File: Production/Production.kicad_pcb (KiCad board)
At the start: 2 copper layers, 8.6 x 4.5 mm, 38 parts, among them IC1 MAX3323EEPE+, J1 530480510, J13 FH34SRJ-16S-0.5SH_50_, J2 530480410, J3 USB4085-GF-A_REVB, J6 Program, U1 BD33FC0FP-E2, U2 ADR02AUJZ-REEL7, U3 ATSAMD21G18A-AUT, Y1 32.768, 12.5pF

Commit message: Solid layout, could be better
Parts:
- removed S1: RESET, PVA1EEH21.2NV2:PVA1EEH212NV2
- removed S2: SET, PVA1EEH21.2NV2:PVA1EEH212NV2
- removed S3: SOFT, PVA1EEH21.2NV2:PVA1EEH212NV2
- added RESET1: B3U-1000P, Button_Switch_SMD:SW_SPST_B3U-1000P, F.Cu at (99.5, 93.5)
- added SET1: TS01-66-73-BK-160-D, TS01-66-73-BK-160-D:TS016673BK160D, F.Cu at (116.8, 68.8)
- added SOFT1: TS01-66-73-BK-160-D, TS01-66-73-BK-160-D:TS016673BK160D, F.Cu at (90.2, 68.8)
- J2: footprint Connector_Molex:Molex_PicoBlade_53048-0410_1x04_P1.25mm_Horizontal -> Connector_Molex_2:Molex_PicoBlade_53048-0410_1x04_P1.25mm_Horizontal
- moved J6 81.1 mm to (89.0, 88.5), turned to 180 degrees
- moved D4 32.3 mm to (99.5, 98.0), turned to -90 degrees
- moved R8 12.2 mm to (96.0, 78.5), turned to 180 degrees
- moved D3 3.64 mm to (113.0, 67.0), turned to -90 degrees
- moved J2 3.00 mm to (96.0, 93.5)
- moved R7 1.00 mm to (101.5, 78.0)
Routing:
- net GND: track 0.00 -> 77.3 mm, vias 0 -> 51
- net SETLED: track 0.00 -> 36.9 mm, vias 0 -> 2
- net Net-(D4-A): track 2.66 -> 30.2 mm
- net SWDIO: track 0.00 -> 24.2 mm, vias 0 -> 1
- net SWCLK: track 0.00 -> 23.9 mm, vias 0 -> 1
- net TXLED: track 19.2 -> 6.46 mm
- net +3V3: track 56.2 -> 67.2 mm, vias 0 -> 1
- net RST: track 0.00 -> 10.3 mm
- net /Net-(D1-A): track 5.56 -> 1.65 mm
- net RUN: track 17.7 -> 20.7 mm
- net TOUT1: track 12.4 -> 15.2 mm
- net RIN1: track 10.2 -> 12.6 mm
- net TIN1: track 14.5 -> 16.8 mm
- net SOFTBTN: track 19.8 -> 21.8 mm
- net OLED_RST: track 14.6 -> 15.8 mm
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- added copper zone on B.Cu, net GND
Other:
- board size 8.6 x 4.5 mm -> 37 x 35 mm

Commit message: Combined TXLED and SETLED
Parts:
- removed D3: LED, LED_SMD:LED_0805_2012Metric
- removed R4: 65, Resistor_SMD:R_0805_2012Metric
- J2: footprint Connector_Molex_2:Molex_PicoBlade_53048-0410_1x04_P1.25mm_Horizontal -> Connector_Molex:Molex_PicoBlade_53048-0410_1x04_P1.25mm_Horizontal
- moved D4 31.6 mm to (113.0, 69.4), turned to 90 degrees
- moved R8 2.34 mm to (98.3, 78.5)
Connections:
- U3 pad 26: TXLED -> SETLED
- U3 pad 39: TXLED -> unconnected-(U3-PA27-Pad39)
- U3 pad 47: SETLED -> unconnected-(U3-PB02-Pad47)
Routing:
- net SETLED: track 36.9 -> 0.00 mm, vias 2 -> 0
- net Net-(D4-A): track 30.2 -> 23.5 mm
- net GND: track 77.3 -> 72.4 mm, vias 51 -> 50
- net TXLED: track 6.46 -> 4.31 mm
- net /Net-(D1-A): track 1.65 -> 0.00 mm

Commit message: I layout
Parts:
- removed J6: Program, Connector_PinSocket_2.54mm:PinSocket_1x04_P2.54mm_Vertical
- added REF**: TestPoint_Pad_D1.5mm, TestPoint:TestPoint_Pad_D1.5mm, B.Cu at (101.5, 84.3)
- added REF**: TestPoint_Pad_D1.5mm, TestPoint:TestPoint_Pad_D1.5mm, B.Cu at (101.5, 89.4)
- added REF**: TestPoint_Pad_D1.5mm, TestPoint:TestPoint_Pad_D1.5mm, B.Cu at (101.5, 86.8)
- added REF**: TestPoint_Pad_D1.5mm, TestPoint:TestPoint_Pad_D1.5mm, B.Cu at (101.5, 81.8)
- C1, C10, C11, C12, C13, C2, C3, C4, C5, C6, C7, C8, C9: footprint Capacitor_SMD:C_0805_2012Metric -> Capacitor_SMD:C_0504_1310Metric
- J2: footprint Connector_Molex:Molex_PicoBlade_53048-0410_1x04_P1.25mm_Horizontal -> Connector_Molex_2:Molex_PicoBlade_53048-0410_1x04_P1.25mm_Horizontal
- R1, R2, R3, R5, R6, R7, R8: footprint Resistor_SMD:R_0805_2012Metric -> Resistor_SMD:R_0603_1608Metric
- RESET1: footprint Button_Switch_SMD:SW_SPST_B3U-1000P -> Button_Switch_SMD:SW_SPST_B3U-3000P; moved to B.Cu
- U2: footprint Package_TO_SOT_SMD:TSOT-23-5_HandSoldering -> Package_TO_SOT_SMD:TSOT-23-5
- moved RESET1 27.2 mm to (105.8, 67.0), turned to 180 degrees
- moved SET1 26.8 mm to (90.0, 67.5)
- moved SOFT1 26.0 mm to (116.2, 67.8)
- moved C4 24.8 mm to (100.2, 86.5), turned to 90 degrees
- moved C13 21.9 mm to (104.2, 93.2)
- moved D2 17.8 mm to (96.5, 90.0)
- moved U1 14.0 mm to (107.8, 88.5), turned to 0 degrees
- moved D4 13.8 mm to (99.2, 70.2), turned to -90 degrees
- moved IC1 12.9 mm to (98.2, 97.2), turned to -90 degrees
- moved R2 11.7 mm to (114.5, 96.2), turned to 0 degrees
- moved C8 10.2 mm to (100.6, 84.0), turned to 180 degrees
- moved R3 9.72 mm to (113.0, 78.2)
- moved R5 9.25 mm to (113.0, 76.8)
- moved C12 8.75 mm to (113.0, 68.8), turned to 180 degrees
- moved C11 8.50 mm to (100.0, 66.0), turned to 180 degrees
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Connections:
- R8 pad 1: TXLED -> SETLED
- U3 pad 12: SETBTN -> SOFTBTN
- U3 pad 13: OLED_RST -> unconnected-(U3-PA08-Pad13)
- U3 pad 14: RUN -> unconnected-(U3-PA09-Pad14)
- U3 pad 23: OLED_DC -> OLED_CS
- U3 pad 24: OLED_CS -> OLED_RST
- U3 pad 25: RS_INVALID -> OLED_DC
- U3 pad 29: SOFTBTN -> SETBTN
- U3 pad 47: unconnected-(U3-PB02-Pad47) -> RUN
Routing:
- net GND: track 72.4 -> 48.2 mm, vias 50 -> 57
- net ROUT1: track 10.3 -> 32.1 mm
- net ZOOM: track 7.07 -> 26.0 mm
- net Net-(D4-A): track 23.5 -> 5.24 mm
- net SWCLK: track 23.9 -> 6.91 mm
- net SWDIO: track 24.2 -> 7.79 mm
- net TIN1: track 16.8 -> 32.5 mm
- net +3V3: track 67.2 -> 53.9 mm
- net SOFTBTN: track 21.8 -> 12.6 mm
- net D-: track 13.7 -> 22.8 mm
- net D+: track 13.7 -> 22.7 mm
- net RST: track 10.3 -> 1.37 mm, vias 0 -> 1
- net VIN: track 25.8 -> 17.9 mm
- net SCK: track 4.59 -> 12.5 mm, vias 0 -> 2
- net TOUT1: track 15.2 -> 9.55 mm
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- added copper zone on F.Cu, net GND
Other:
- board size 37 x 35 mm -> 38.5 x 37 mm

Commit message: Changing power regulator
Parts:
- moved RESET1 31.7 mm to (89.8, 94.4), turned to -90 degrees
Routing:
- net RST: track 1.37 -> 39.5 mm
- net GND: track 48.2 -> 56.3 mm, vias 57 -> 56
- net +3V3: track 53.9 -> 56.8 mm
- net TIN1: track 32.5 -> 34.5 mm
- net ROUT1: track 32.1 -> 33.8 mm
- net SCK: track 12.5 -> 11.0 mm
- net MOSI: track 8.98 -> 7.83 mm
- net +24V: track 44.4 -> 45.5 mm
- net VUSB: track 13.4 -> 14.4 mm
- net /Net-(J8-CC2): track 12.7 -> 13.6 mm

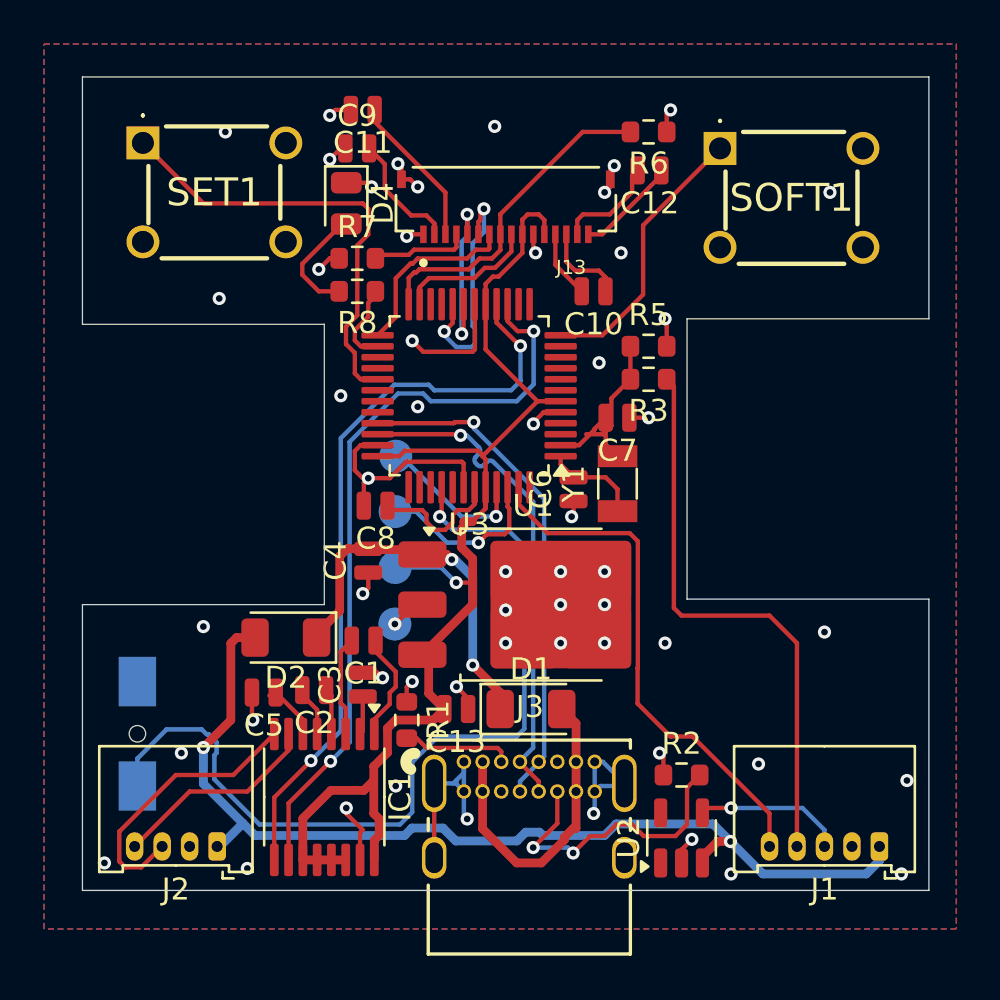
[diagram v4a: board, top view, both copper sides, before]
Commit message: Pretty solid I redesign
Rotated mcu and reassigned pins for better layout, swapped ldo
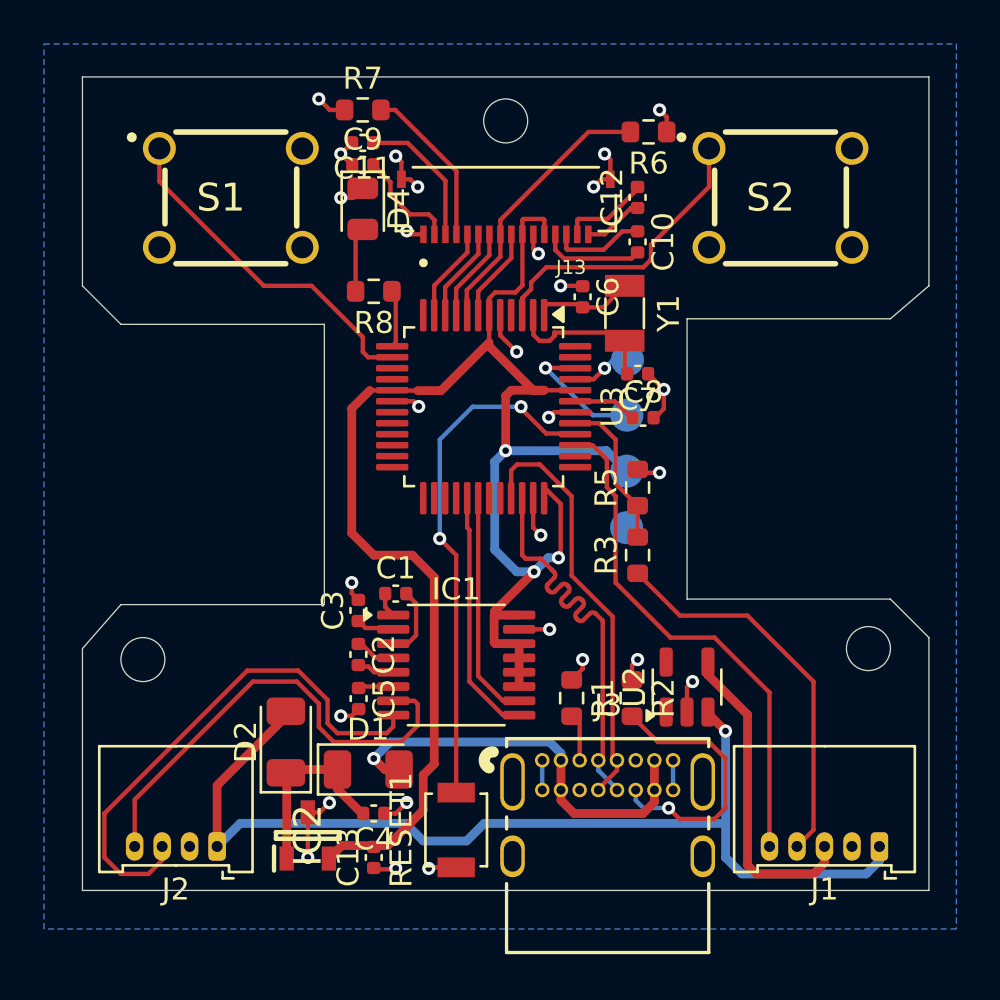
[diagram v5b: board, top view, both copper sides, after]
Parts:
- removed SET1, SOFT1: TS01-66-73-BK-160-D, TS01-66-73-BK-160-D:TS016673BK160D
- removed U1: BD33FC0FP-E2, Package_TO_SOT_SMD:TO-252-3_TabPin2
- added IC2: AP7375-33SA-7, AP7375-33SA-7:SOT96P240X110-3N, F.Cu at (97.5, 99.0)
- added S1: FSM12JH, FSM10JH:FSM4JH, F.Cu at (94.0, 70.0)
- added S2: FSM12JH, FSM10JH:FSM4JH, F.Cu at (119.0, 70.0)
- C1, C10, C11, C12, C2, C3, C5, C6, C7, C8, C9: footprint Capacitor_SMD:C_0504_1310Metric -> Capacitor_SMD:C_0402_1005Metric
- C13: value 20uF,60V+ -> 10uF,10V+; footprint Capacitor_SMD:C_0504_1310Metric -> Capacitor_SMD:C_0402_1005Metric
- C4: value 20uF,60V+ -> 1uF,60V+; footprint Capacitor_SMD:C_0504_1310Metric -> Capacitor_SMD:C_0402_1005Metric
- RESET1: footprint Button_Switch_SMD:SW_SPST_B3U-3000P -> Button_Switch_SMD:SW_SPST_B3U-1000P; moved to F.Cu
- moved RESET1 15.1 mm to (104.2, 98.8), turned to 90 degrees
- moved C8 12.8 mm to (112.8, 80.0), turned to 0 degrees
- moved C4 11.5 mm to (100.5, 98.0), turned to 180 degrees
- moved REF** 11.4 mm to (112.0, 85.0)
- moved REF** 11.4 mm to (112.0, 77.4)
- moved REF** 11.4 mm to (112.0, 79.9)
- moved REF** 11.4 mm to (112.0, 82.4)
- moved C6 8.76 mm to (110.0, 74.5), turned to -90 degrees
- moved IC1 8.49 mm to (104.2, 91.2), turned to 0 degrees
- moved R3 8.02 mm to (112.5, 86.2), turned to 90 degrees
- moved D1 7.89 mm to (100.2, 96.0)
- moved Y1 7.76 mm to (111.9, 75.2), turned to -90 degrees
- moved C13 7.72 mm to (100.5, 100.0), turned to 90 degrees
- moved R1 7.57 mm to (109.5, 92.8)
- moved U2 6.87 mm to (114.8, 92.2)
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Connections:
- U3 pad 10: unconnected-(U3-PA05-Pad10) -> SCK
- U3 pad 11: unconnected-(U3-PA06-Pad11) -> MOSI
- U3 pad 12: SOFTBTN -> unconnected-(U3-PA07-Pad12)
- U3 pad 13: unconnected-(U3-PA08-Pad13) -> SETLED
- U3 pad 14: unconnected-(U3-PA09-Pad14) -> SETBTN
- U3 pad 15: TIN1 -> unconnected-(U3-PA10-Pad15)
- U3 pad 16: ROUT1 -> unconnected-(U3-PA11-Pad16)
- U3 pad 19: MOSI -> unconnected-(U3-PB10-Pad19)
- U3 pad 20: SCK -> unconnected-(U3-PB11-Pad20)
- U3 pad 23: OLED_CS -> unconnected-(U3-PA14-Pad23)
- U3 pad 24: OLED_RST -> unconnected-(U3-PA15-Pad24)
- U3 pad 25: OLED_DC -> unconnected-(U3-PA16-Pad25)
- U3 pad 26: SETLED -> unconnected-(U3-PA17-Pad26)
- U3 pad 29: SETBTN -> ROUT1
- U3 pad 3: ZSIG -> SOFTBTN
- U3 pad 30: unconnected-(U3-PA21-Pad30) -> TIN1
- U3 pad 39: unconnected-(U3-PA27-Pad39) -> RUN
- U3 pad 41: USBHOSTEN -> ZSIG
- U3 pad 47: RUN -> unconnected-(U3-PB02-Pad47)
- U3 pad 7: unconnected-(U3-PB08-Pad7) -> OLED_CS
- U3 pad 8: unconnected-(U3-PB09-Pad8) -> OLED_RST
- U3 pad 9: unconnected-(U3-PA04-Pad9) -> OLED_DC
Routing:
- net TIN1: track 34.5 -> 10.4 mm, vias 2 -> 0
- net ROUT1: track 33.8 -> 11.3 mm, vias 2 -> 0
- net +3V3: track 56.8 -> 76.1 mm, vias 1 -> 3
- net GND: track 56.3 -> 38.6 mm, vias 56 -> 28
- net RST: track 39.5 -> 23.7 mm, vias 1 -> 2
- net TOUT1: track 9.55 -> 21.5 mm
- net RIN1: track 12.7 -> 24.1 mm
- net VIN: track 17.4 -> 8.79 mm, vias 2 -> 0
- net ZOOM: track 26.0 -> 17.9 mm
- net ZREF: track 6.81 -> 14.6 mm, vias 1 -> 0
- net SCK: track 11.0 -> 4.31 mm, vias 2 -> 0
- net SETBTN: track 20.7 -> 15.8 mm
- net SWCLK: track 7.04 -> 2.24 mm
- net VUSB: track 14.4 -> 19.1 mm, vias 0 -> 1
- net OLED_DC: track 8.40 -> 4.31 mm
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- removed copper zone on F.Cu, net GND
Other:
- outline, holes or cut-outs redrawn
